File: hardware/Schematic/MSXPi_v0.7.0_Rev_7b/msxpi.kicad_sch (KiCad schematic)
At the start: 36 parts, among them IC1 LD117A, J1 ROM_SWITCH, U1 28C256

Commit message: Starting routing - before chnaging pin assigments support more clean routing traces
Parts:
- EPM3064ALC44: renamed from EPM3064ALC1; value (none) -> EPM3064ALC44; footprint (none) -> msxpi:PLCC-S44
- JP1: value (none) -> MSXCART1; footprint (none) -> Roni Footprints:MSX_CART
- JP2: footprint (none) -> msxpi:2X05_90
- R2, R3, R4: footprint (none) -> msxpi:0207_7
- R8: value R-US_0207/7 -> 470
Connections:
- net SPI_SCLK is gone; now on net SPI_CLK: R8.2

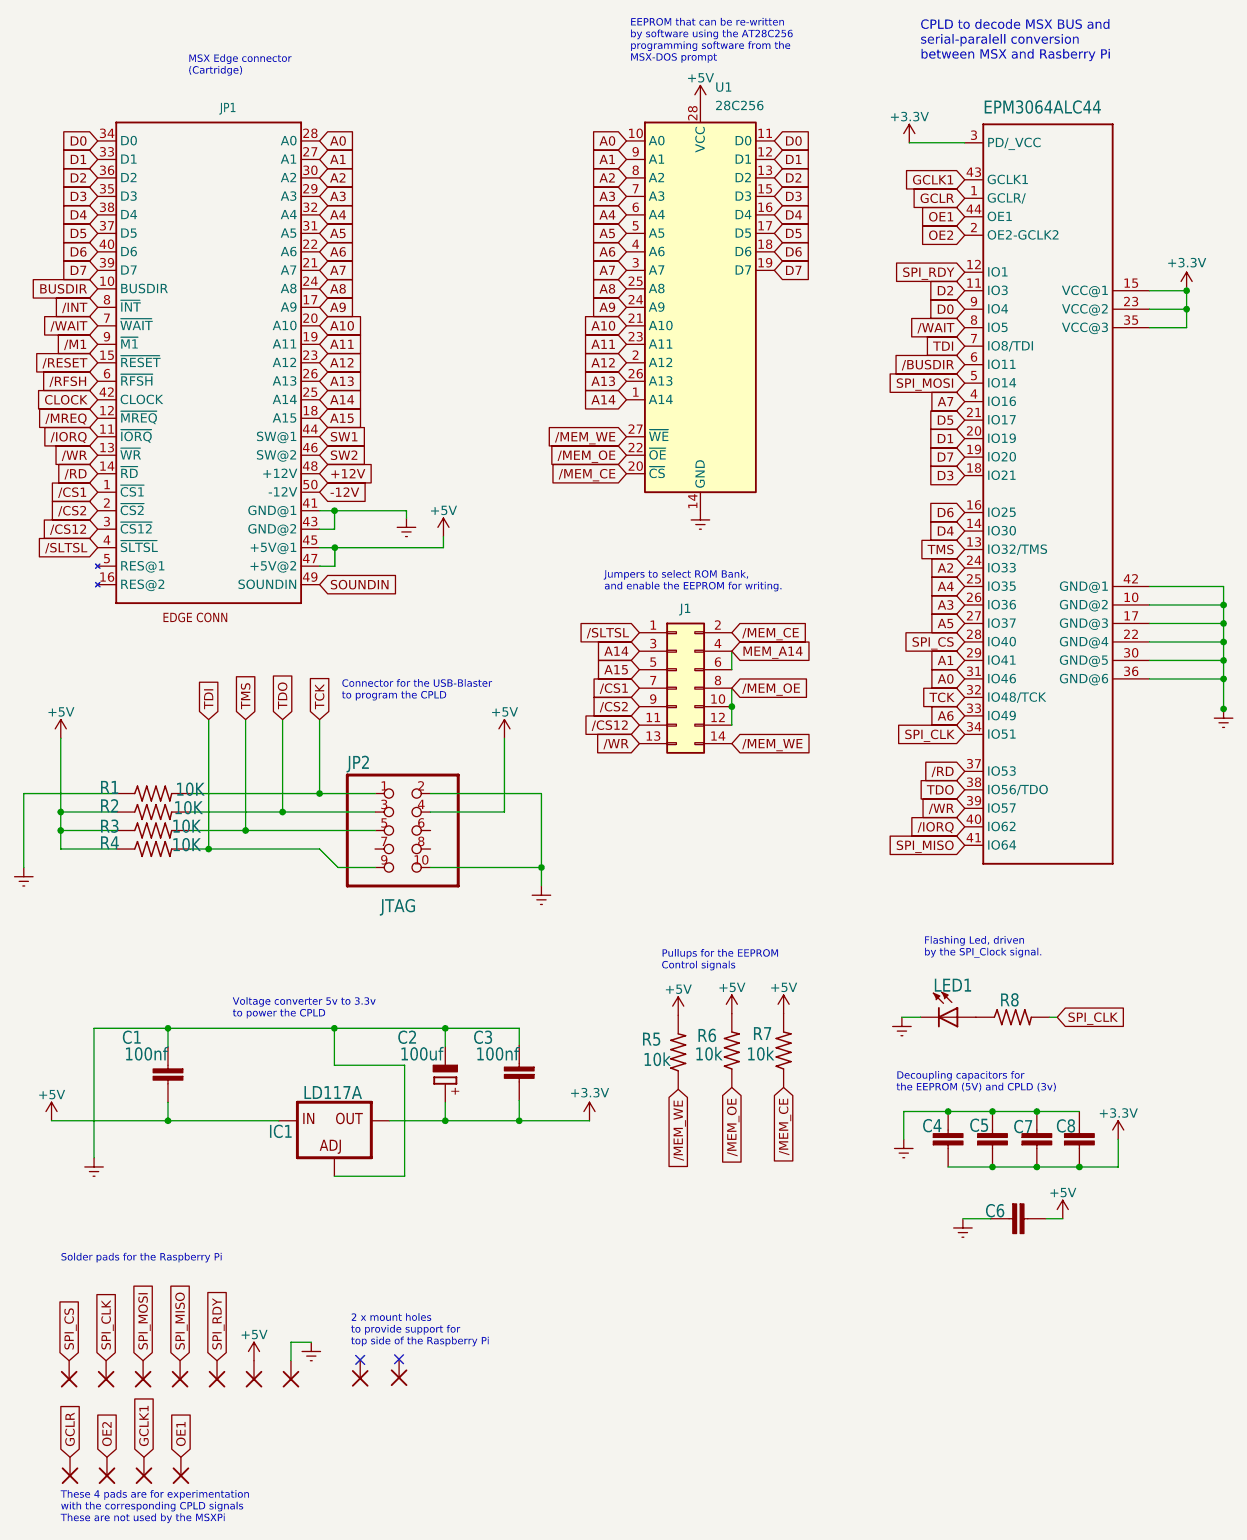
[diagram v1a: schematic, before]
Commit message: routing complete. need to update footprint for ld1117
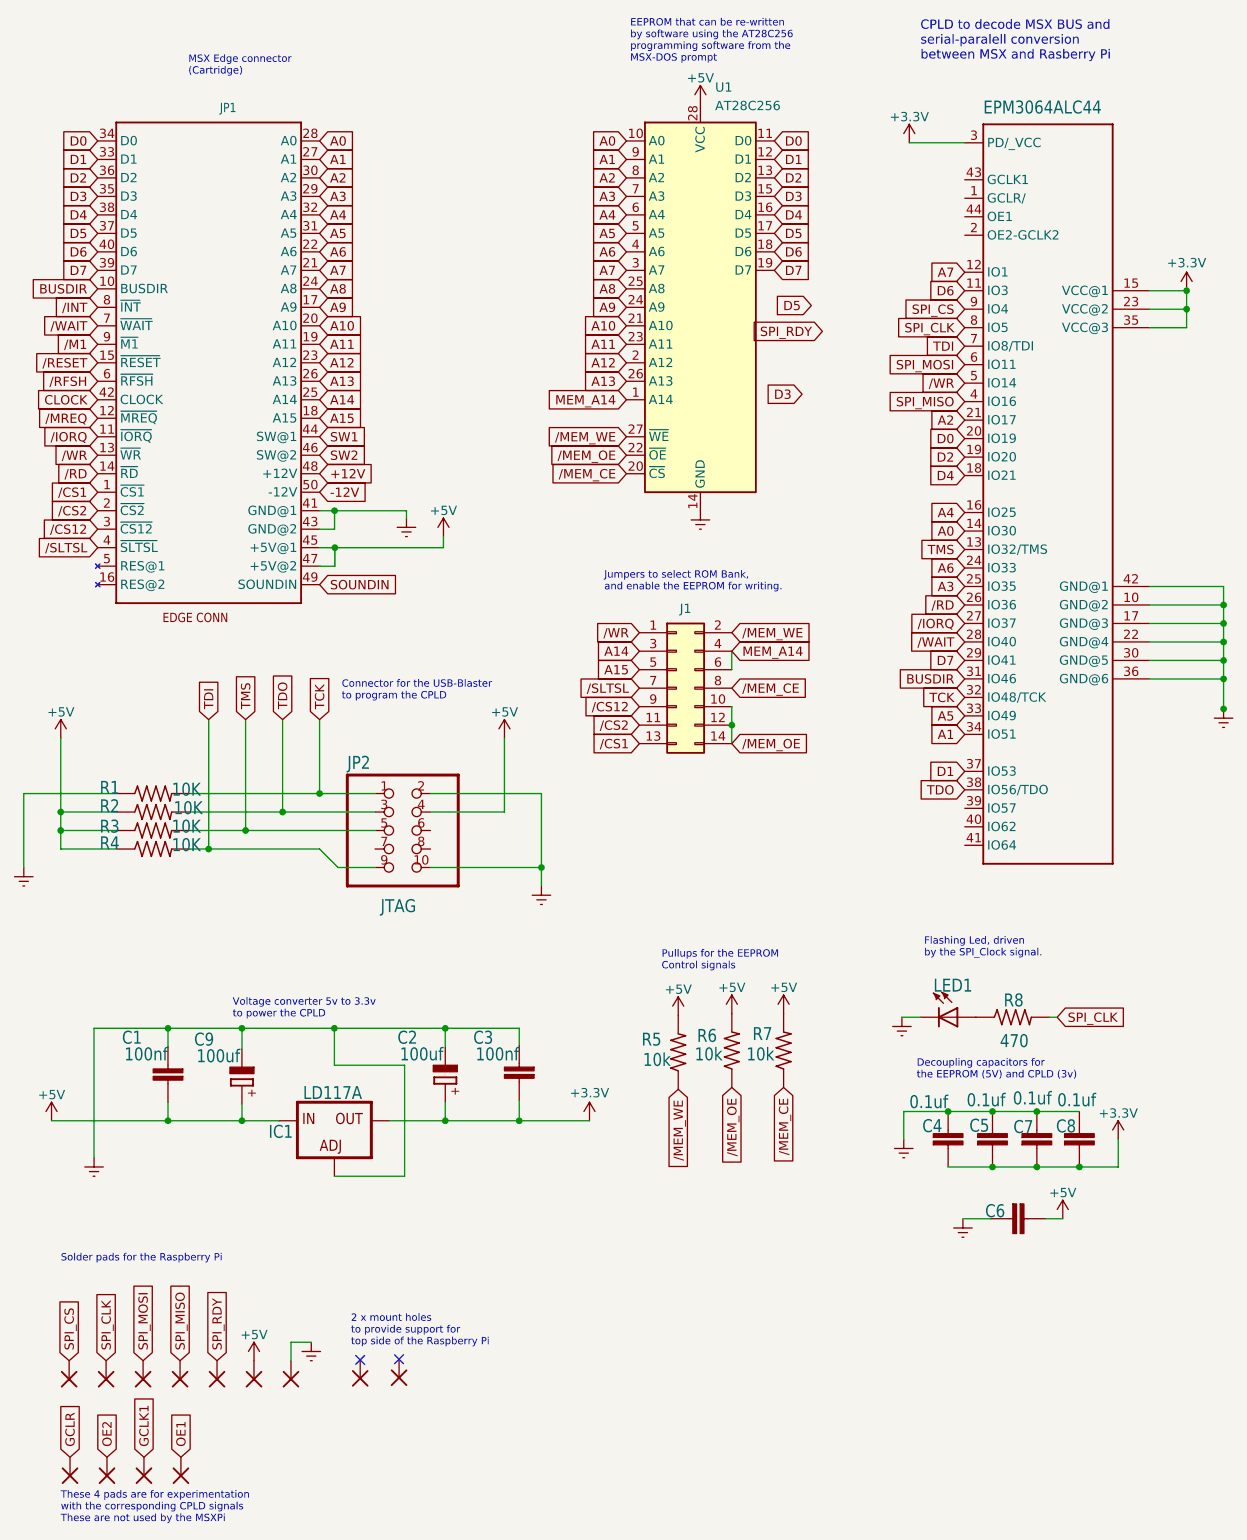
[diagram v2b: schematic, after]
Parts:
- added C9: 100uf, msxpi:E2,5-5, symbol msxpi-eagle-import:CPOL-EUE2.5-5
- C4, C5, C6, C7, C8: value C2,5-3 -> 0.1uf
- IC1: footprint msxpi:TO220L1 -> Package_TO_SOT_SMD:SOT-223-3_TabPin2
- U1: value 28C256 -> AT28C256
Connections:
- net /BUSDIR is gone; now on net SPI_MOSI: EPM3064ALC44.6 (IO11)
- net +5V: now also C9.+
- net A0: now also EPM3064ALC44.14 (IO30); no longer EPM3064ALC44.31 (IO46)
- net A1: now also EPM3064ALC44.34 (IO51); no longer EPM3064ALC44.29 (IO41)
- net A14: no longer U1.1 (A14)
- net A2: now also EPM3064ALC44.21 (IO17); no longer EPM3064ALC44.24 (IO33)
- net A3: now also EPM3064ALC44.25 (IO35); no longer EPM3064ALC44.26 (IO36)
- net A4: now also EPM3064ALC44.16 (IO25); no longer EPM3064ALC44.25 (IO35)
- net A5: now also EPM3064ALC44.33 (IO49); no longer EPM3064ALC44.27 (IO37)
- net A6: now also EPM3064ALC44.24 (IO33); no longer EPM3064ALC44.33 (IO49)
- net A7: now also EPM3064ALC44.12 (IO1); no longer EPM3064ALC44.4 (IO16)
- net BUSDIR: now also EPM3064ALC44.31 (IO46)
- net D0: now also EPM3064ALC44.20 (IO19); no longer EPM3064ALC44.9 (IO4)
- net D1: now also EPM3064ALC44.37 (IO53); no longer EPM3064ALC44.20 (IO19)
- net D2: now also EPM3064ALC44.19 (IO20); no longer EPM3064ALC44.11 (IO3)
- net D3: no longer EPM3064ALC44.18 (IO21)
- net D4: now also EPM3064ALC44.18 (IO21); no longer EPM3064ALC44.14 (IO30)
- net D5: no longer EPM3064ALC44.21 (IO17)
- net D6: now also EPM3064ALC44.11 (IO3); no longer EPM3064ALC44.16 (IO25)
- net D7: now also EPM3064ALC44.29 (IO41); no longer EPM3064ALC44.19 (IO20)
- net GCLK1: no longer EPM3064ALC44.43 (GCLK1)
- net GCLR: no longer EPM3064ALC44.1 (GCLR/)
- net GNDREF: now also C9.-
- net MEM_A14: now also U1.1 (A14)
- net OE1: no longer EPM3064ALC44.44 (OE1)
- net OE2: no longer EPM3064ALC44.2 (OE2-GCLK2)
- net SPI_CLK: now also EPM3064ALC44.8 (IO5); no longer EPM3064ALC44.34 (IO51)
- net SPI_CS: now also EPM3064ALC44.9 (IO4); no longer EPM3064ALC44.28 (IO40)
- net SPI_MISO: now also EPM3064ALC44.4 (IO16); no longer EPM3064ALC44.41 (IO64)
- net SPI_MOSI: no longer EPM3064ALC44.5 (IO14)
- net SPI_RDY: no longer EPM3064ALC44.12 (IO1)
- net /CS1: now also J1.13 (Pin_13); no longer J1.7 (Pin_7)
- net /CS12: now also J1.9 (Pin_9); no longer J1.11 (Pin_11)
- net /CS2: now also J1.11 (Pin_11); no longer J1.9 (Pin_9)
- net /IORQ: now also EPM3064ALC44.27 (IO37); no longer EPM3064ALC44.40 (IO62)
- net /MEM_CE: now also J1.8 (Pin_8); no longer J1.2 (Pin_2)
- net /MEM_OE: now also J1.14 (Pin_14); no longer J1.8 (Pin_8)
- net /MEM_WE: now also J1.2 (Pin_2); no longer J1.14 (Pin_14)
- net /RD: now also EPM3064ALC44.26 (IO36); no longer EPM3064ALC44.37 (IO53)
- net /SLTSL: now also J1.7 (Pin_7); no longer J1.1 (Pin_1)
- net /WAIT: now also EPM3064ALC44.28 (IO40); no longer EPM3064ALC44.8 (IO5)
- net /WR: now also EPM3064ALC44.5 (IO14), J1.1 (Pin_1); no longer EPM3064ALC44.39 (IO57), J1.13 (Pin_13)

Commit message: Almost ready for fabrication. Need to add logo and credits
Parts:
- JP2: footprint msxpi:2X05_90 -> Connector_PinHeader_2.54mm:PinHeader_2x05_P2.54mm_Vertical
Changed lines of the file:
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@@
       (effects (font (size 1.778 1.5113)) (justify left bottom))
     )
-    (property "Footprint" "msxpi:2X05_90" (id 2) (at 61.214 115.824 0)
+    (property "Footprint" "Connector_PinHeader_2.54mm:PinHeader_2x05_P2.54mm_Vertical" (id 2) (at 61.214 115.824 0)
       (effects (font (size 1.27 1.27)) hide)
     )
@@
     )
     (path "/610fb86f-39b8-496e-b00e-193fd857bffc"
-      (reference "JP2") (unit 1) (value "JTAG") (footprint "msxpi:2X05_90")
+      (reference "JP2") (unit 1) (value "JTAG") (footprint "Connector_PinHeader_2.54mm:PinHeader_2x05_P2.54mm_Vertical")
     )
     (path "/0044612c-4860-4f3b-9000-ca145b60660d"
